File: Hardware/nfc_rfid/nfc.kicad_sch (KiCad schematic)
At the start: 48 parts, among them IC1 ST25R3916-AQWT, J1 BW0033AG-L3.4W0.9H1.8, J2 BW0033AG-L3.4W0.9H1.8, Y1 CF4027M12010001

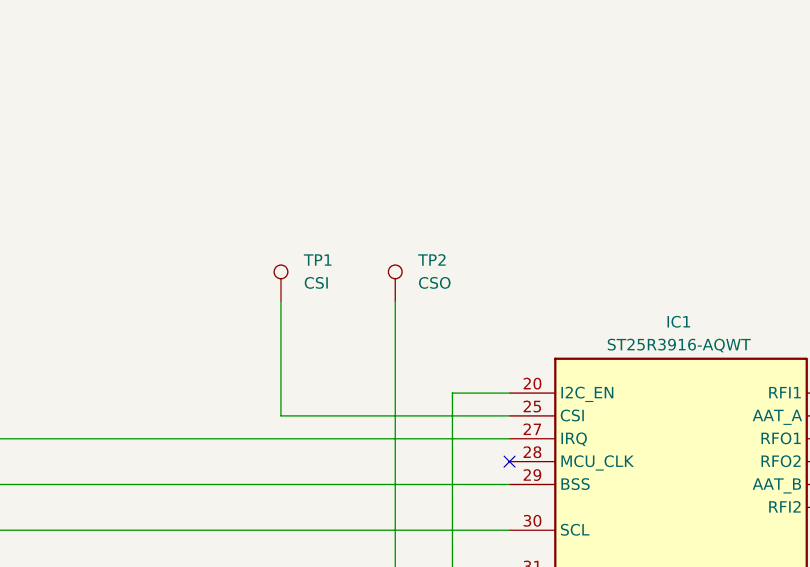
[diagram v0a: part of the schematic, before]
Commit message: PCB: Components placing done
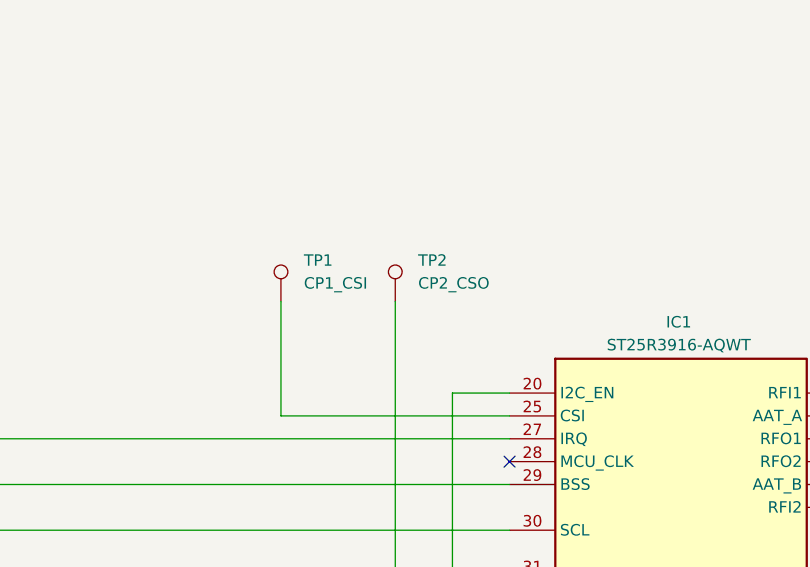
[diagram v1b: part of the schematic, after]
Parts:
- L1, L2: footprint Inductor_SMD:L_0402_1005Metric -> Inductor_SMD:L_0805_2012Metric
- TP1: value CSI -> CP1_CSI
- TP2: value CSO -> CP2_CSO
- Y1: footprint Crystal:Crystal_SMD_3225-4Pin_3.2x2.5mm -> Crystal:Crystal_SMD_2016-4Pin_2.0x1.6mm
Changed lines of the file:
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@@
 			)
 		)
-		(property "Value" "CSI"
+		(property "Value" "CP1_CSI"
 			(at 107.95 100.8379 0)
 			(effects
@@
 			)
 		)
-		(property "Footprint" "Inductor_SMD:L_0402_1005Metric"
+		(property "Footprint" "Inductor_SMD:L_0805_2012Metric"
 			(at 234.95 69.85 0)
 			(effects
@@
 			)
 		)
-		(property "Footprint" "Inductor_SMD:L_0402_1005Metric"
+		(property "Footprint" "Inductor_SMD:L_0805_2012Metric"
 			(at 234.95 102.87 0)
 			(effects
@@
 			)
 		)
-		(property "Value" "CSO"
+		(property "Value" "CP2_CSO"
 			(at 120.65 100.8379 0)
 			(effects
@@
 			)
 		)
-		(property "Footprint" "Crystal:Crystal_SMD_3225-4Pin_3.2x2.5mm"
+		(property "Footprint" "Crystal:Crystal_SMD_2016-4Pin_2.0x1.6mm"
 			(at 111.76 153.67 0)
 			(effects

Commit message: PCB: add "remove from bom" entity; adjust design rule
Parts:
- TP1, TP2, TP3, TP4, TP5: now left out of the parts list
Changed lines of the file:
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@@
 		(unit 1)
 		(exclude_from_sim no)
-		(in_bom yes)
+		(in_bom no)
 		(on_board yes)
 		(dnp no)
@@
 		(unit 1)
 		(exclude_from_sim no)
-		(in_bom yes)
+		(in_bom no)
 		(on_board yes)
 		(dnp no)
@@
 		(unit 1)
 		(exclude_from_sim no)
-		(in_bom yes)
+		(in_bom no)
 		(on_board yes)
 		(dnp no)
@@
 		(unit 1)
 		(exclude_from_sim no)
-		(in_bom yes)
+		(in_bom no)
 		(on_board yes)
 		(dnp no)
@@
 		(unit 1)
 		(exclude_from_sim no)
-		(in_bom yes)
+		(in_bom no)
 		(on_board yes)
 		(dnp no)
